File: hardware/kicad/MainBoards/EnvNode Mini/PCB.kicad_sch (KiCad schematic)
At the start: 4 parts

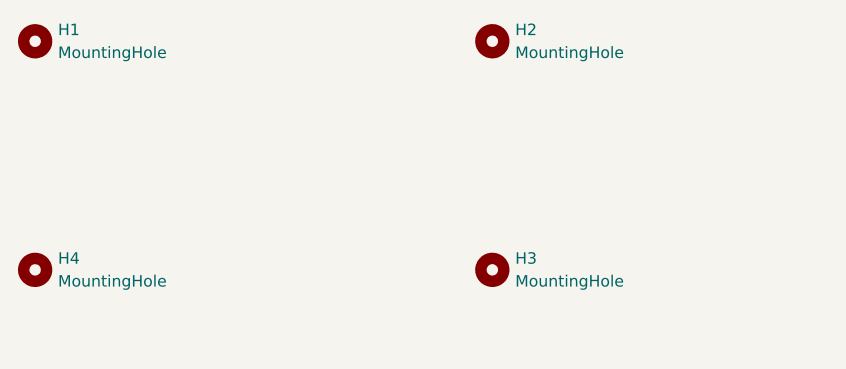
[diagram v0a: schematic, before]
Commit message: feat(hardware): complete EnvNode Mini revision 0.6
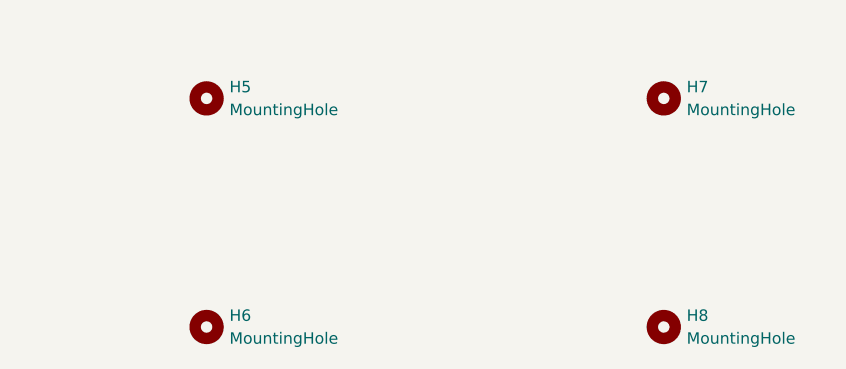
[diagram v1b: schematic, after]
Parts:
- renumbered H1 to H5, H4 to H6, H2 to H7, H3 to H8
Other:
- moved on the sheet: H5, H6, H7, H8
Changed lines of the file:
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@@
 	(symbol
 		(lib_id "Mechanical:MountingHole")
-		(at 127 88.9 0)
+		(at 146.05 95.25 0)
 		(unit 1)
 		(body_style 1)
@@
 		(dnp no)
 		(fields_autoplaced yes)
-		(property "Reference" "H3"
-			(at 129.54 87.6299 0)
+		(property "Reference" "H8"
+			(at 148.59 93.9799 0)
 			(show_name no)
 			(do_not_autoplace no)
@@
 		)
 		(property "Value" "MountingHole"
-			(at 129.54 90.1699 0)
+			(at 148.59 96.5199 0)
 			(show_name no)
 			(do_not_autoplace no)
@@
 		)
 		(property "Footprint" "EnvNode-Footprints:MountingHole_4.5mm_SelfTapping_4mm"
-			(at 127 88.9 0)
+			(at 146.05 95.25 0)
 			(hide yes)
 			(show_name no)
@@
 		)
 		(property "Datasheet" ""
-			(at 127 88.9 0)
+			(at 146.05 95.25 0)
 			(hide yes)
 			(show_name no)
@@
 		)
 		(property "Description" "BOX4U mounting hole: NPTH 4.5 mm for 4 mm self-tapping screw"
-			(at 127 88.9 0)
+			(at 146.05 95.25 0)
 			(hide yes)
 			(show_name no)
@@
 				)
 			)
+			(project "EnvNode Mini"
+				(path "/bb35dba2-ff1a-441b-885c-8dff8d3b7ea1/b5fd6d73-aa5b-4f44-9fa4-96bd08cd097d"
+					(reference "H8")
+					(unit 1)
+				)
+			)
 		)
 	)
 	(symbol
 		(lib_id "Mechanical:MountingHole")
-		(at 127 63.5 0)
+		(at 146.05 69.85 0)
 		(unit 1)
 		(body_style 1)
@@
 		(dnp no)
 		(fields_autoplaced yes)
-		(property "Reference" "H2"
-			(at 129.54 62.2299 0)
+		(property "Reference" "H7"
+			(at 148.59 68.5799 0)
 			(show_name no)
 			(do_not_autoplace no)
@@
 		)
 		(property "Value" "MountingHole"
-			(at 129.54 64.7699 0)
+			(at 148.59 71.1199 0)
 			(show_name no)
 			(do_not_autoplace no)
@@
 		)
 		(property "Footprint" "EnvNode-Footprints:MountingHole_4.5mm_SelfTapping_4mm"
-			(at 127 63.5 0)
+			(at 146.05 69.85 0)
 			(hide yes)
 			(show_name no)
@@
 		)
 		(property "Datasheet" ""
-			(at 127 63.5 0)
+			(at 146.05 69.85 0)
 			(hide yes)
 			(show_name no)
@@
 		)
 		(property "Description" "BOX4U mounting hole: NPTH 4.5 mm for 4 mm self-tapping screw"
-			(at 127 63.5 0)
+			(at 146.05 69.85 0)
 			(hide yes)
 			(show_name no)
@@
 				)
 			)
+			(project "EnvNode Mini"
+				(path "/bb35dba2-ff1a-441b-885c-8dff8d3b7ea1/b5fd6d73-aa5b-4f44-9fa4-96bd08cd097d"
+					(reference "H7")
+					(unit 1)
+				)
+			)
 		)
 	)
 	(symbol
 		(lib_id "Mechanical:MountingHole")
-		(at 76.2 63.5 0)
+		(at 95.25 69.85 0)
 		(unit 1)
 		(body_style 1)
@@
 		(dnp no)
 		(fields_autoplaced yes)
-		(property "Reference" "H1"
-			(at 78.74 62.2299 0)
+		(property "Reference" "H5"
+			(at 97.79 68.5799 0)
 			(show_name no)
 			(do_not_autoplace no)
@@
 		)
 		(property "Value" "MountingHole"
-			(at 78.74 64.7699 0)
+			(at 97.79 71.1199 0)
 			(show_name no)
 			(do_not_autoplace no)
@@
 		)
 		(property "Footprint" "EnvNode-Footprints:MountingHole_4.5mm_SelfTapping_4mm"
-			(at 76.2 63.5 0)
+			(at 95.25 69.85 0)
 			(hide yes)
 			(show_name no)
@@
 		)
 		(property "Datasheet" ""
-			(at 76.2 63.5 0)
+			(at 95.25 69.85 0)
 			(hide yes)
 			(show_name no)
@@
 		)
 		(property "Description" "BOX4U mounting hole: NPTH 4.5 mm for 4 mm self-tapping screw"
-			(at 76.2 63.5 0)
+			(at 95.25 69.85 0)
 			(hide yes)
 			(show_name no)
@@
 				)
 			)
+			(project "EnvNode Mini"
+				(path "/bb35dba2-ff1a-441b-885c-8dff8d3b7ea1/b5fd6d73-aa5b-4f44-9fa4-96bd08cd097d"
+					(reference "H5")
+					(unit 1)
+				)
+			)
 		)
 	)
 	(symbol
 		(lib_id "Mechanical:MountingHole")
-		(at 76.2 88.9 0)
+		(at 95.25 95.25 0)
 		(unit 1)
 		(body_style 1)
@@
 		(dnp no)
 		(fields_autoplaced yes)
-		(property "Reference" "H4"
-			(at 78.74 87.6299 0)
+		(property "Reference" "H6"
+			(at 97.79 93.9799 0)
 			(show_name no)
 			(do_not_autoplace no)
@@
 		)
 		(property "Value" "MountingHole"
-			(at 78.74 90.1699 0)
+			(at 97.79 96.5199 0)
 			(show_name no)
 			(do_not_autoplace no)
@@
 		)
 		(property "Footprint" "EnvNode-Footprints:MountingHole_4.5mm_SelfTapping_4mm"
-			(at 76.2 88.9 0)
+			(at 95.25 95.25 0)
 			(hide yes)
 			(show_name no)
@@
 		)
 		(property "Datasheet" ""
-			(at 76.2 88.9 0)
+			(at 95.25 95.25 0)
 			(hide yes)
 			(show_name no)
@@
 		)
 		(property "Description" "BOX4U mounting hole: NPTH 4.5 mm for 4 mm self-tapping screw"
-			(at 76.2 88.9 0)
+			(at 95.25 95.25 0)
 			(hide yes)
 			(show_name no)
@@
 				)
 			)
-		)
-	)
+			(project "EnvNode Mini"
+				(path "/bb35dba2-ff1a-441b-885c-8dff8d3b7ea1/b5fd6d73-aa5b-4f44-9fa4-96bd08cd097d"
+					(reference "H6")
+					(unit 1)
+				)
+			)
+		)
+	)
+	(group "BOX4U-5U210900"
+		(lib_id "EnvNodeDesignBlocks:BOX4U-5U210900")
+		(members "19c47de5-0a93-40cb-bd83-f3618e053454" "41841eb0-bd6a-44e8-9bd2-e3d455bf7d30"
+			"8c10209e-677b-48af-b82c-12a960c32134" "d70d6959-eb9c-4897-876f-77e77489979f"
+		)
+	)
